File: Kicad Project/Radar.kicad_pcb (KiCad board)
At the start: 2 copper layers, 104.1 x 101.6 mm, 50 parts, among them U1 GALI-1+, U10 GALI-2+, U11 BandpassFilter, U13 Antenna111, U14 Antenna111, U2 MCA1-85L+, U3 BandpassFilter, U4 LMV751, U5 LMV751, U6 GALI-2+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

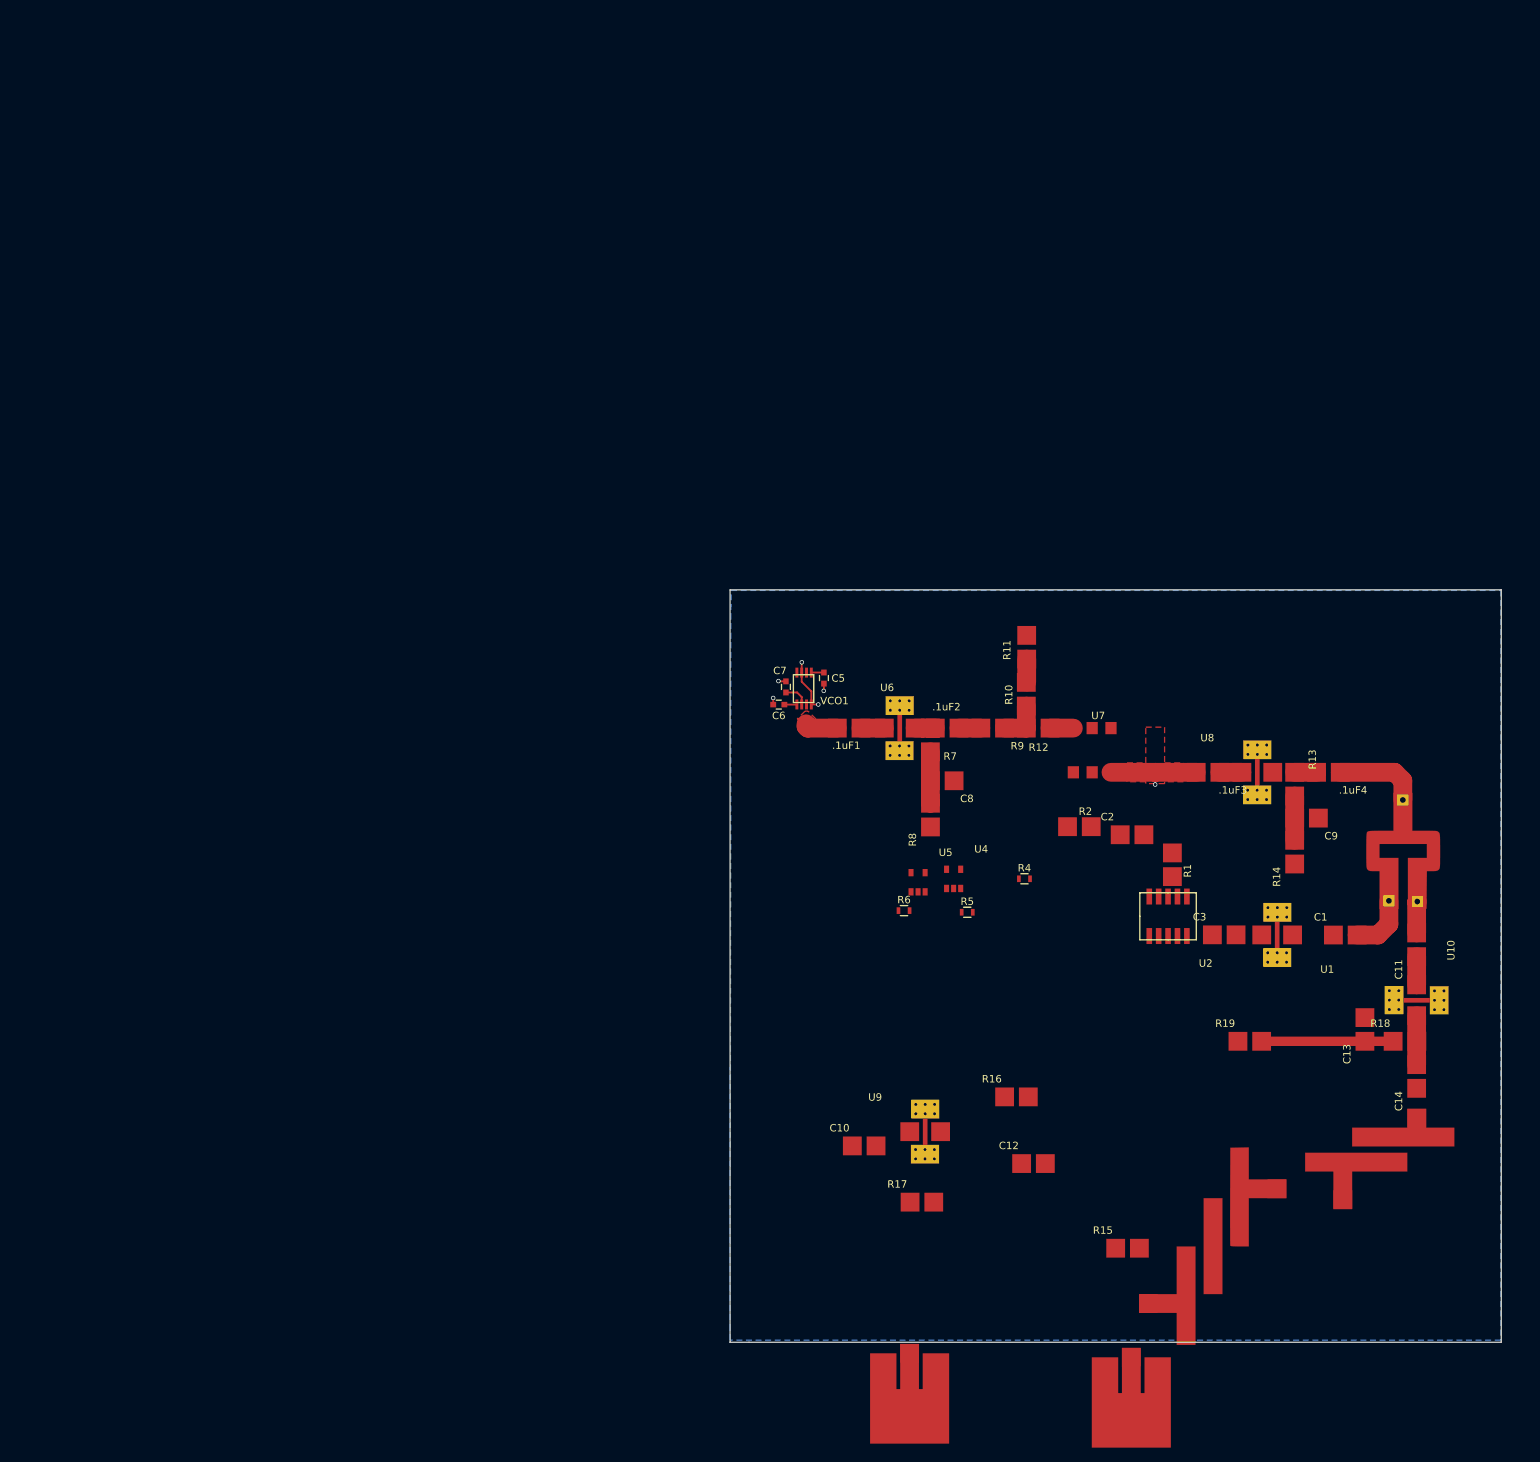
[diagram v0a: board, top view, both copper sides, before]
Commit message: Connected patch antennas, removed cap on rx side, added radial stub
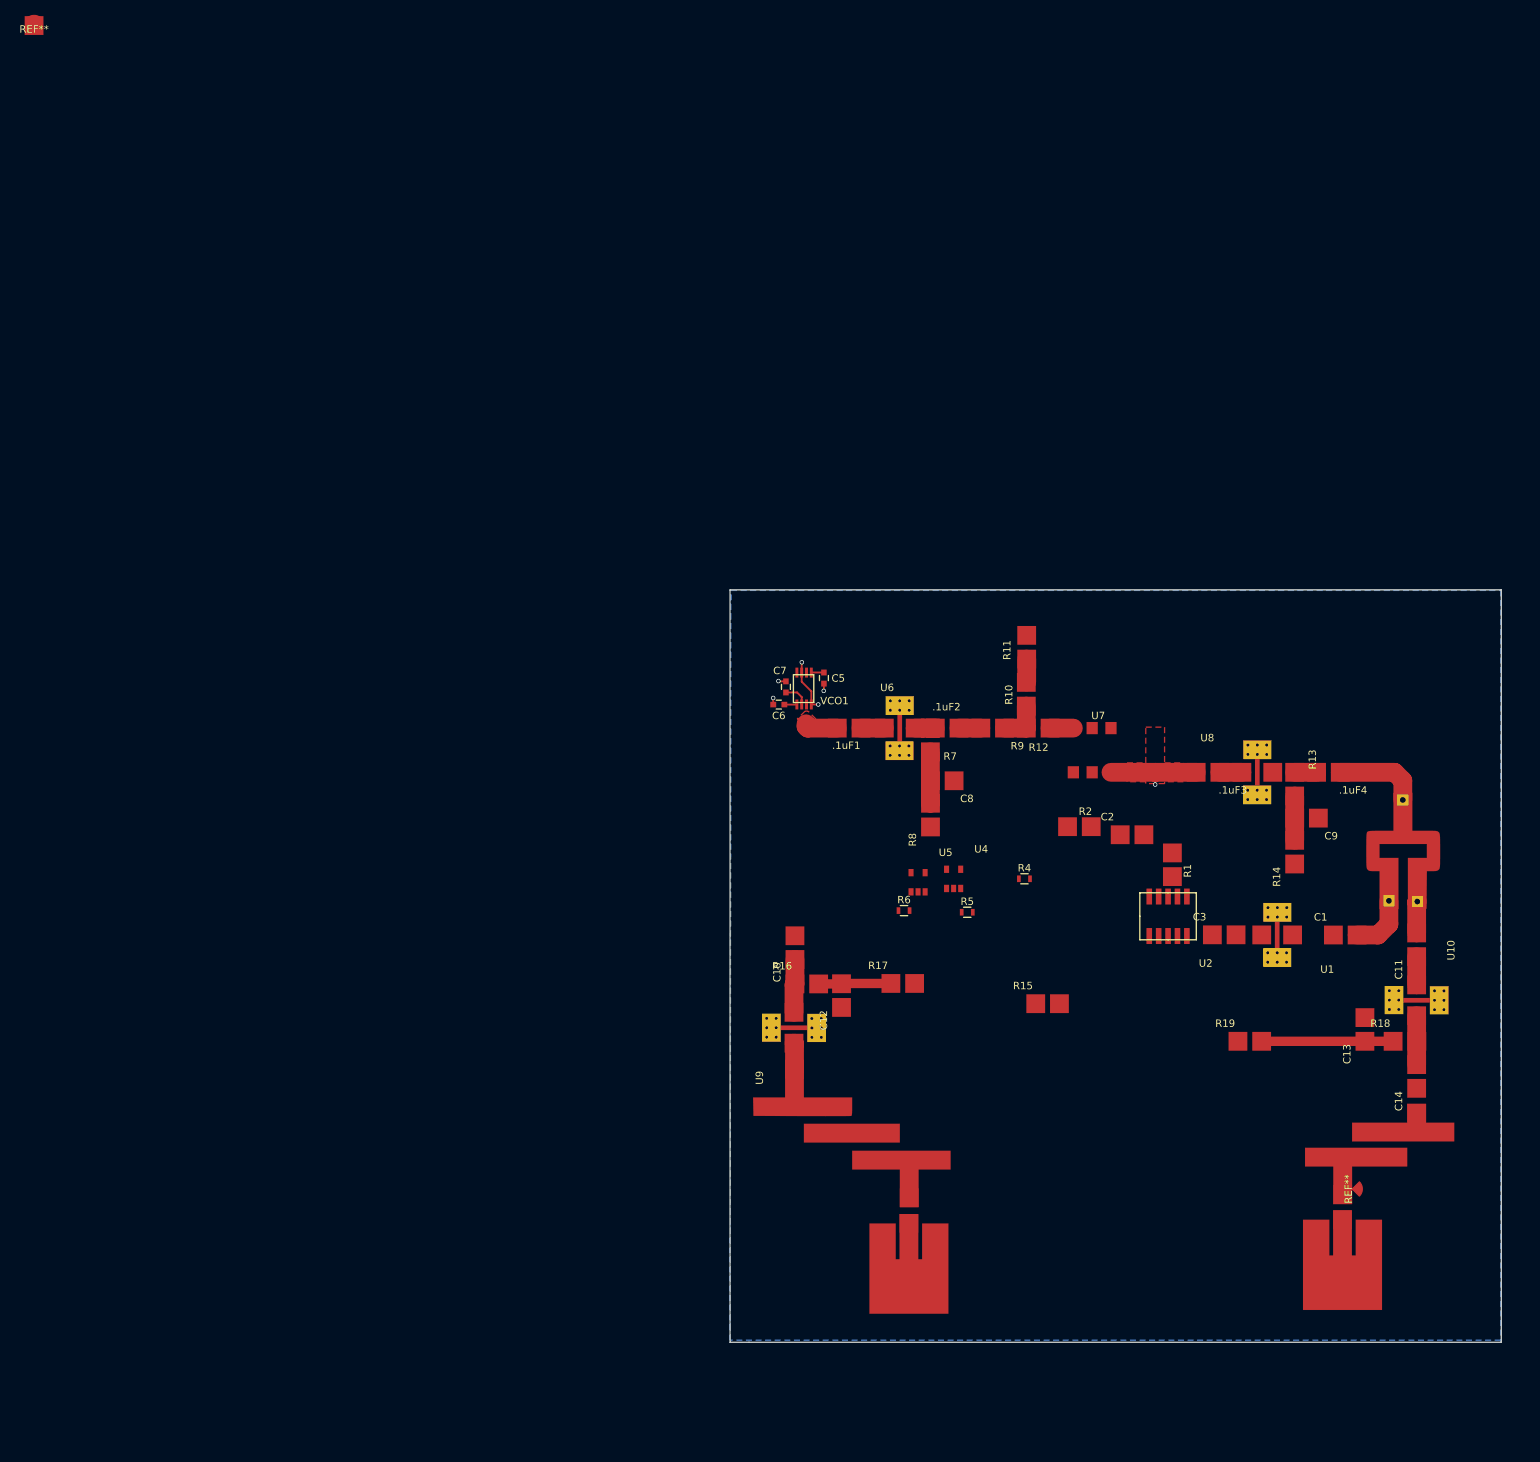
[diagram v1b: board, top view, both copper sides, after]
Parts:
- added REF**: muwave_arcstub, muwave_arcstub, F.Cu at (178.0, 157.1)
- added REF**: muwave_arcstub, muwave_arcstub, F.Cu at (0.00, 0.00)
- moved U3 50.5 mm to (110.6, 150.0), turned to 90 degrees
- moved R15 34.7 mm to (136.5, 133.3)
- moved U14 34.0 mm to (174.6, 169.3)
- moved C12 33.9 mm to (110.3, 131.3), turned to 90 degrees
- moved R16 32.2 mm to (104.0, 130.7)
- moved R17 29.6 mm to (117.0, 130.6)
- moved C10 28.8 mm to (104.0, 124.8), turned to 90 degrees
- moved U9 21.3 mm to (103.9, 136.1), turned to 90 degrees
- moved U13 17.5 mm to (116.0, 169.8)
- moved U11 0.67 mm to (180.8, 155.0)
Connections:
- U3 pad 2: Net-(C4-Pad1) -> Net-(U3-Pad2)
- U9 pad 1: Net-(C4-Pad2) -> Net-(U3-Pad2)
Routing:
- net Net-(C12-Pad2): track 0.00 -> 9.78 mm
- net Net-(C10-Pad1): track 0.00 -> 7.19 mm
- net Net-(U3-Pad2): track 0.00 -> 3.56 mm

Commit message: PCB
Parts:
- removed U5: LMV751, RadarComponents:SOT23-5
- added C15: 270pF, Capacitors_SMD:C_0603, F.Cu at (145.8, 112.9)
- added C16: 270pF, Capacitors_SMD:C_0603, F.Cu at (137.1, 108.9)
- added C4: 270pF, Capacitors_SMD:C_0603, F.Cu at (130.1, 114.7)
- added R3: 47k, Resistors_SMD:R_0603, F.Cu at (132.2, 112.9)
- R4: value 100 -> 10k
- R5: value 100k -> 100
- R6: value 10k -> 100k
- moved REF** 251.9 mm to (165.8, 189.6)
- moved R6 20.0 mm to (137.0, 115.5), turned to 180 degrees
- moved R2 19.1 mm to (159.9, 109.4)
- moved R5 16.9 mm to (141.5, 112.9)
- moved U4 14.1 mm to (136.7, 111.0), turned to 270 degrees
- moved C2 13.7 mm to (160.6, 115.6)
- moved R1 10.2 mm to (161.3, 118.1)
- moved R4 0.91 mm to (133.0, 114.7), turned to 270 degrees
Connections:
- R4 pad 1: Net-(R4-Pad1) -> Net-(C4-Pad1)
- R4 pad 2: Net-(R4-Pad2) -> GND
- R5 pad 2: Net-(R4-Pad1) -> Net-(C15-Pad1)
- R6 pad 1: Net-(R6-Pad1) -> Net-(R5-Pad1)
- U10 pad 1: Net-(C11-Pad1) -> (no net)
- U10 pad 2: GND -> (no net)
- U10 pad 3: Net-(C14-Pad2) -> (no net)
- U11 pad 2: Net-(0ohms2-Pad2) -> (no net)
- U2 pad 3: Net-(R4-Pad2) -> Net-(C15-Pad2)
- U3 pad 2: Net-(U3-Pad2) -> (no net)
- U4 pad 1: Net-(R5-Pad1) -> Net-(R6-Pad2)
- U4 pad 3: Net-(R4-Pad1) -> Net-(C4-Pad1)
- U4 pad 4: GND -> Net-(R5-Pad1)
- U9 pad 1: Net-(U3-Pad2) -> (no net)
- U9 pad 2: GND -> (no net)
- U9 pad 3: Net-(C10-Pad1) -> (no net)
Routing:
- net Net-(C15-Pad2): track 0.00 -> 10.4 mm
- net (no net): track 0.00 -> 10.4 mm
- net Net-(C2-Pad2): track 0.00 -> 8.95 mm
- net GND: track 23.6 -> 30.3 mm, vias 6 -> 9
- net Net-(C14-Pad2): track 6.60 -> 0.00 mm
- net Net-(C3-Pad2): track 0.00 -> 6.37 mm
- net Net-(C4-Pad1): track 0.00 -> 6.16 mm
- net Net-(R6-Pad2): track 0.00 -> 5.69 mm
- net Net-(C1-Pad1): track 0.00 -> 5.52 mm
- net Net-(R5-Pad1): track 0.00 -> 5.52 mm
- net Net-(U3-Pad2): track 3.56 -> 0.00 mm
- net Net-(C15-Pad1): track 0.00 -> 2.79 mm
- net +9V: track 0.00 -> 2.09 mm
- added copper zone on F.Cu, net Net-(C15-Pad2)

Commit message: PCB Changes
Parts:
- removed .1uF1, .1uF2, .1uF3: C, RadarComponents:100PAD
- removed REF** (x2): muwave_arcstub, muwave_arcstub
- added 0ohms1: R, RadarComponents:100PAD, F.Cu at (125.2, 164.1)
- added 0ohms2: R, RadarComponents:100PAD, F.Cu at (173.4, 164.2)
- added C17: 10uF, Capacitors_SMD:C_0805, F.Cu at (117.2, 114.6)
- added C18: C, RadarComponents:100PAD, F.Cu at (106.9, 93.6)
- added C19: C, Capacitors_SMD:C_0805, F.Cu at (114.7, 119.1)
- added C20: C, RadarComponents:100PAD, F.Cu at (123.4, 93.6)
- added C21: C, RadarComponents:100PAD, F.Cu at (158.6, 99.6)
- added J1: Conn_01x02, Pin_Headers:Pin_Header_Straight_1x02_Pitch1.27mm, F.Cu at (96.9, 103.0)
- added J2: Conn_01x02, Pin_Headers:Pin_Header_Straight_1x02_Pitch1.27mm, F.Cu at (96.9, 112.4)
- added J3: Conn_01x02, Pin_Headers:Pin_Header_Straight_1x02_Pitch1.27mm, F.Cu at (96.9, 106.2)
- added J4: Conn_01x02, RadarComponents:UFL, F.Cu at (133.0, 85.1)
- added J5: Conn_01x02, Pin_Headers:Pin_Header_Straight_1x02_Pitch1.27mm, F.Cu at (96.9, 109.3)
- added R20: R, Resistors_SMD:R_0603, F.Cu at (109.3, 117.0)
- added U12: ufl, RadarComponents:UFL, F.Cu at (112.3, 162.9)
- added U15: ufl, RadarComponents:UFL, F.Cu at (161.5, 156.5)
- added U5: AP1117-50, RadarComponents:ZLDO1117, F.Cu at (104.0, 110.1)
- C12, C2, C8, C9, R18, R19: footprint RadarComponents:100PAD -> RadarComponents:100PAD+GND2
- R15: footprint RadarComponents:100PAD -> Resistors_SMD:R_0603
- moved U14 60.3 mm to (114.6, 175.4)
- moved U13 49.5 mm to (165.2, 174.8)
- moved R15 31.3 mm to (112.1, 113.7)
- moved R19 4.79 mm to (167.9, 135.9), turned to 180 degrees
- moved C8 3.43 mm to (119.9, 102.2), turned to 0 degrees
- moved U6 3.43 mm to (112.6, 96.1)
- moved C2 3.39 mm to (161.3, 112.3), turned to 180 degrees
- moved R18 3.02 mm to (185.5, 135.5), turned to 180 degrees
- moved R8 2.59 mm to (119.9, 106.0)
- moved C9 2.47 mm to (171.5, 108.1), turned to 0 degrees
- moved R7 2.41 mm to (117.3, 96.1)
- moved R11 1.60 mm to (135.3, 82.7), turned to 0 degrees
- moved C5 0.72 mm to (106.0, 88.4)
- moved VCO1 0.72 mm to (103.1, 88.4)
- moved C6 0.72 mm to (99.9, 91.9)
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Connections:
- R15 pad 2: Net-(R15-Pad2) -> GND
- U10 pad 1: (no net) -> Net-(C11-Pad1)
- U10 pad 2: (no net) -> GND
- U10 pad 3: (no net) -> Net-(C14-Pad2)
- U11 pad 2: (no net) -> Net-(0ohms2-Pad2)
- U3 pad 2: (no net) -> Net-(U3-Pad2)
- U9 pad 1: (no net) -> Net-(U3-Pad2)
- U9 pad 2: (no net) -> GND
- U9 pad 3: (no net) -> Net-(C10-Pad1)
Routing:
- net Net-(C13-Pad1): track 17.8 -> 0.00 mm
- net +5V: track 0.00 -> 17.1 mm
- net Net-(J4-Pad2): track 3.10 -> 12.9 mm
- net (no net): track 10.4 -> 0.59 mm
- net +9V: track 2.09 -> 11.2 mm
- net Net-(C8-Pad2): track 6.95 -> 0.00 mm
- net Net-(C12-Pad2): track 9.78 -> 3.06 mm
- net GND: track 30.3 -> 36.5 mm
- net Net-(C18-Pad2): track 4.67 -> 0.00 mm
- net Net-(U3-Pad2): track 0.00 -> 3.56 mm
- net Net-(C20-Pad2): track 2.72 -> 5.97 mm
- net +3V3: track 5.09 -> 7.44 mm
- removed copper zone on F.Cu, net Net-(C20-Pad2)

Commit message: More PCB Updates
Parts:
- added J6: Conn_01x02, Pin_Headers:Pin_Header_Straight_1x02_Pitch1.27mm, F.Cu at (91.1, 111.8)
- C13, R14, R2, R8: footprint RadarComponents:100PAD -> RadarComponents:100PAD+GND
- R18: footprint RadarComponents:100PAD+GND2 -> RadarComponents:100PAD+GND
- U3: footprint RadarComponents:QuadPoleFilter -> RadarComponents:QuadPoleFilterMirror
- moved C19 45.0 mm to (69.9, 123.5)
- moved 0ohms2 36.1 mm to (146.2, 188.0), turned to 0 degrees
- moved R20 33.6 mm to (76.3, 122.8)
- moved 0ohms1 31.8 mm to (146.2, 188.0), turned to 0 degrees
- moved C17 31.4 mm to (86.1, 110.1)
- moved U9 20.0 mm to (123.7, 133.3)
- moved C10 19.7 mm to (123.7, 123.3)
- moved R16 17.7 mm to (121.1, 126.2), turned to 180 degrees
- moved U14 13.5 mm to (104.8, 166.1)
- moved U13 12.7 mm to (174.7, 166.3)
- moved U15 12.5 mm to (174.0, 155.1), turned to 90 degrees
- moved U12 11.4 mm to (104.1, 154.9), turned to 90 degrees
- moved R17 8.03 mm to (110.2, 126.2), turned to 180 degrees
- moved R19 7.21 mm to (174.6, 133.2)
- moved U3 5.76 mm to (114.8, 146.1)
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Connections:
- C13 pad 1: Net-(C13-Pad1) -> GND
- C13 pad 2: GND -> Net-(C13-Pad2)
- R18 pad 1: Net-(C13-Pad1) -> Net-(C13-Pad2)
- R19 pad 2: Net-(C13-Pad1) -> Net-(C13-Pad2)
- U11 pad 2: Net-(0ohms2-Pad2) -> Net-(U11-Pad2)
- U12 pad 1: Net-(0ohms1-Pad2) -> Net-(U12-Pad1)
- U13 pad 1: Net-(0ohms2-Pad1) -> Net-(U11-Pad2)
- U14 pad 1: Net-(0ohms1-Pad1) -> Net-(U12-Pad1)
- U15 pad 1: Net-(0ohms2-Pad2) -> Net-(U11-Pad2)
- U3 pad 1: Net-(0ohms1-Pad2) -> Net-(U12-Pad1)
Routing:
- net +9V: track 11.2 -> 88.5 mm
- net RFIN: track 0.00 -> 28.9 mm
- net Net-(C13-Pad2): track 0.00 -> 13.7 mm
- net GND: track 36.5 -> 29.1 mm
- net Net-(C8-Pad2): track 0.00 -> 5.90 mm
- net Net-(C12-Pad2): track 3.06 -> 7.67 mm
- net Net-(C14-Pad1): track 0.00 -> 3.72 mm
- net Net-(C3-Pad2): track 6.37 -> 3.12 mm
- net Net-(C3-Pad1): track 0.00 -> 3.12 mm
- net Net-(C18-Pad2): track 0.00 -> 3.00 mm
- net Net-(.1uF4-Pad2): track 2.96 -> 5.92 mm
- net Net-(C2-Pad2): track 8.95 -> 7.19 mm
- net Net-(C10-Pad1): track 7.19 -> 8.84 mm
- net PowerSplitter: track 12.3 -> 10.8 mm
- net Net-(C15-Pad2): track 10.4 -> 9.59 mm
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- removed copper zone on B.Cu, net GND
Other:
- board size 104.1 x 101.6 mm -> 104.4 x 101.7 mm

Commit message: PCB Pre Flood
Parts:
- added J7: Conn_01x02, Pin_Headers:Pin_Header_Straight_1x02_Pitch1.27mm, F.Cu at (97.9, 101.3)
- added REF**: muwave_stub, RadarComponents:muwave_stub, F.Cu at (150.9, 113.4)
- R17: footprint RadarComponents:100PAD -> RadarComponents:100PAD+GND
- R18: footprint RadarComponents:100PAD+GND -> RadarComponents:100PAD
- moved C19 36.2 mm to (105.0, 115.1), turned to 270 degrees
- moved J6 32.8 mm to (123.9, 110.4), turned to 90 degrees
- moved R20 27.9 mm to (102.8, 114.3), turned to 90 degrees
- moved C17 25.6 mm to (111.3, 114.7)
- moved R15 11.3 mm to (101.3, 116.6), turned to 270 degrees
- moved J1 1.80 mm to (97.9, 104.5)
- moved J2 1.80 mm to (97.9, 113.9)
- moved J3 1.80 mm to (97.9, 107.6)
- moved J5 1.80 mm to (97.9, 110.8)
- moved U5 1.80 mm to (105.0, 111.6)
- moved R17 0.72 mm to (109.6, 125.9)
- moved C13 0.40 mm to (177.5, 135.4)
- moved C20 0.40 mm to (123.3, 93.2)
- moved C4 0.40 mm to (129.9, 114.4)
- moved J4 0.40 mm to (132.8, 84.7)
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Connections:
- R17 pad 1: Net-(C12-Pad2) -> +9V
- R17 pad 2: +9V -> Net-(C12-Pad2)
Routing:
- net +9V: track 88.5 -> 134.6 mm, vias 0 -> 2
- net +5V: track 17.1 -> 32.9 mm
- net Net-(J6-Pad2): track 5.31 -> 15.6 mm
- net Net-(C14-Pad2): track 0.00 -> 5.99 mm
- net Net-(C13-Pad2): track 13.7 -> 7.73 mm
- net Net-(R15-Pad1): track 0.00 -> 5.45 mm
- net Net-(C18-Pad2): track 3.00 -> 6.94 mm
- net Net-(C20-Pad2): track 5.97 -> 9.04 mm
- net +3V3: track 7.44 -> 4.55 mm
- net Net-(C15-Pad2): track 9.59 -> 10.3 mm
- removed copper zone on F.Cu, net Net-(C15-Pad2)
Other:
- board size 104.4 x 101.7 mm -> 100 x 100 mm

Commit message: Added GND Flood
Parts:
- removed 0ohms1, 0ohms2: R, RadarComponents:100PAD
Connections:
- U2 pad 2: (no net) -> GND
- U2 pad 4: (no net) -> GND
- U2 pad 6: (no net) -> GND
- U2 pad 7: (no net) -> GND
- U2 pad 8: (no net) -> GND
- U2 pad 9: (no net) -> GND
- U7 pad 3: (no net) -> GND
- U7 pad 5: (no net) -> GND
- U7 pad 6: (no net) -> GND
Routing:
- net GND: track 29.1 -> 139.4 mm, vias 9 -> 52
- net +9V: track 134.6 -> 148.7 mm
- added copper zone on B.Cu, net GND
